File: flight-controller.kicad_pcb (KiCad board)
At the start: 4 copper layers, 36 x 36 mm, 51 parts, among them J1 USB_C_Receptacle_USB2.0, J2 ESC, J3 RX, J4 GPS, J5 I2C, J6 Camera, J7 VTX, J8 DVTX, U1 AT32F435RGT7

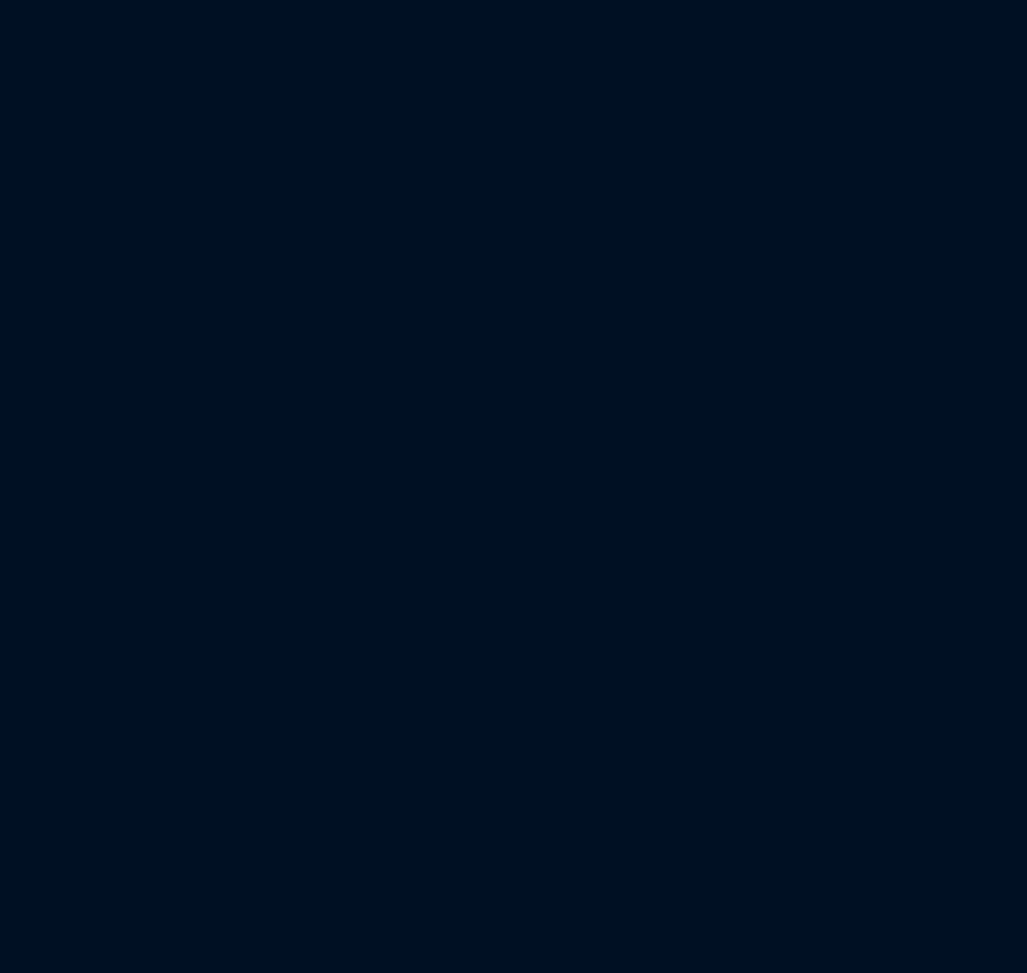
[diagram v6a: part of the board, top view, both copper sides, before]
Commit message: Change baro to I2C
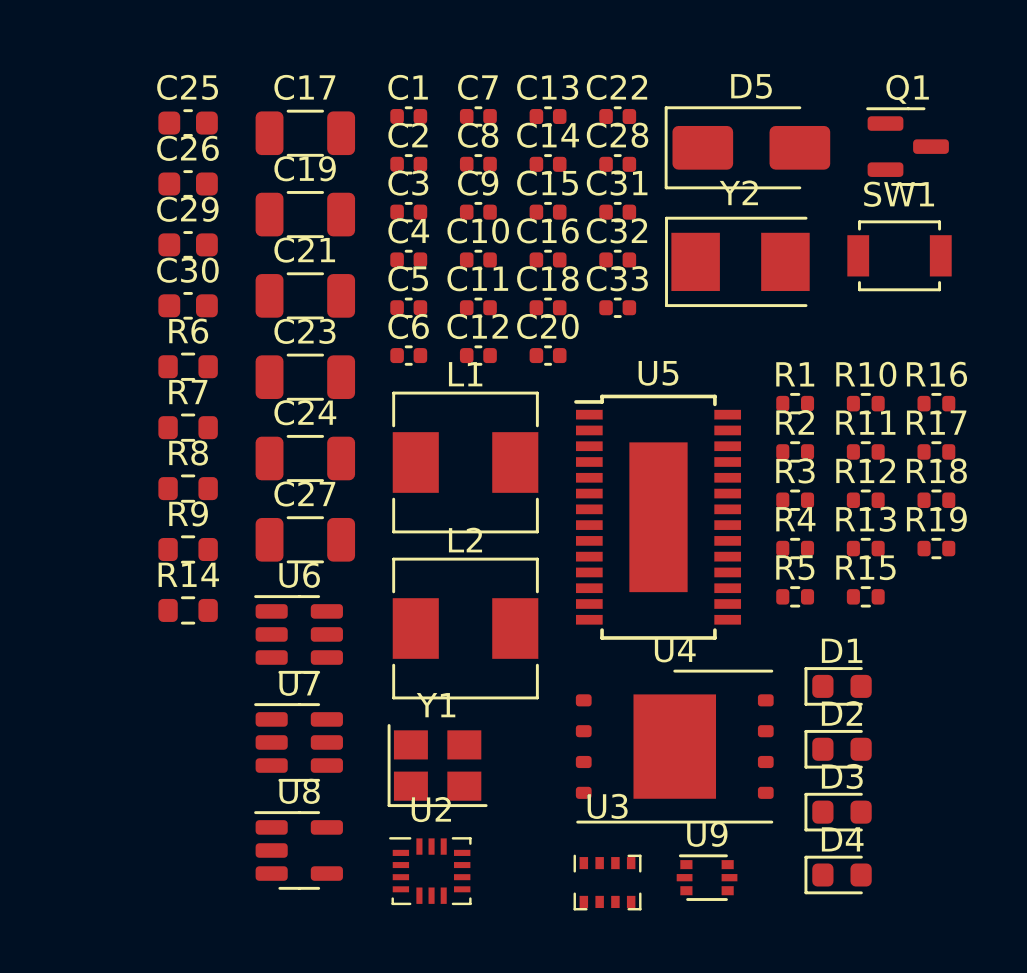
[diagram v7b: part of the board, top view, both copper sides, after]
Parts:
- added C1: 100n, Capacitor_SMD:C_0402_1005Metric, F.Cu at (156.4, 87.8)
- added C10: 100n, Capacitor_SMD:C_0402_1005Metric, F.Cu at (159.2, 93.7)
- added C11: 100n, Capacitor_SMD:C_0402_1005Metric, F.Cu at (159.2, 95.6)
- added C12: 100n, Capacitor_SMD:C_0402_1005Metric, F.Cu at (159.2, 97.6)
- added C13: 100n, Capacitor_SMD:C_0402_1005Metric, F.Cu at (162.1, 87.8)
- added C14: 100n, Capacitor_SMD:C_0402_1005Metric, F.Cu at (162.1, 89.7)
- added C15: 100n, Capacitor_SMD:C_0402_1005Metric, F.Cu at (162.1, 91.7)
- added C16: 68p, Capacitor_SMD:C_0402_1005Metric, F.Cu at (162.1, 93.7)
- added C17: 22u, Capacitor_SMD:C_1206_3216Metric, F.Cu at (152.1, 88.4)
- added C18: 100n, Capacitor_SMD:C_0402_1005Metric, F.Cu at (162.1, 95.6)
- added C19: 10u 50V, Capacitor_SMD:C_1206_3216Metric, F.Cu at (152.1, 91.8)
- added C2: 100n, Capacitor_SMD:C_0402_1005Metric, F.Cu at (156.4, 89.7)
- added C20: 100n, Capacitor_SMD:C_0402_1005Metric, F.Cu at (162.1, 97.6)
- added C21: 10u 50V, Capacitor_SMD:C_1206_3216Metric, F.Cu at (152.1, 95.1)
- added C22: 68p, Capacitor_SMD:C_0402_1005Metric, F.Cu at (165.0, 87.8)
- added C23: 22u, Capacitor_SMD:C_1206_3216Metric, F.Cu at (152.1, 98.5)
- added C24: 22u, Capacitor_SMD:C_1206_3216Metric, F.Cu at (152.1, 101.8)
- added C25: 10u, Capacitor_SMD:C_0603_1608Metric, F.Cu at (147.3, 88.0)
- added C26: 10u, Capacitor_SMD:C_0603_1608Metric, F.Cu at (147.3, 90.5)
- added C27: 22u, Capacitor_SMD:C_1206_3216Metric, F.Cu at (152.1, 105.2)
- added C28: 100n, Capacitor_SMD:C_0402_1005Metric, F.Cu at (165.0, 89.7)
- added C29: 10u, Capacitor_SMD:C_0603_1608Metric, F.Cu at (147.3, 93.0)
- added C3: 100n, Capacitor_SMD:C_0402_1005Metric, F.Cu at (156.4, 91.7)
- added C30: 10u, Capacitor_SMD:C_0603_1608Metric, F.Cu at (147.3, 95.5)
- added C31: 100n, Capacitor_SMD:C_0402_1005Metric, F.Cu at (165.0, 91.7)
- added C32: 22pf, Capacitor_SMD:C_0402_1005Metric, F.Cu at (165.0, 93.7)
- added C33: 22pf, Capacitor_SMD:C_0402_1005Metric, F.Cu at (165.0, 95.6)
- added C4: 100n, Capacitor_SMD:C_0402_1005Metric, F.Cu at (156.4, 93.7)
- added C5: 100n, Capacitor_SMD:C_0402_1005Metric, F.Cu at (156.4, 95.6)
- added C6: 100n, Capacitor_SMD:C_0402_1005Metric, F.Cu at (156.4, 97.6)
- added C7: 100n, Capacitor_SMD:C_0402_1005Metric, F.Cu at (159.2, 87.8)
- added C8: 100n, Capacitor_SMD:C_0402_1005Metric, F.Cu at (159.2, 89.7)
- added C9: 100n, Capacitor_SMD:C_0402_1005Metric, F.Cu at (159.2, 91.7)
- added D1: BLUE, LED_SMD:LED_0603_1608Metric, F.Cu at (174.2, 111.2)
- added D2: GREEN, LED_SMD:LED_0603_1608Metric, F.Cu at (174.2, 113.8)
- added D3: RED, LED_SMD:LED_0603_1608Metric, F.Cu at (174.2, 116.4)
- added D4: YELLOW, LED_SMD:LED_0603_1608Metric, F.Cu at (174.2, 119.0)
- added D5: SS34, Diode_SMD:D_SMA, F.Cu at (170.5, 89.0)
- added L1: 10u, Inductor_SMD:L_Sunlord_MWSA0503S, F.Cu at (158.7, 102.0)
- added L2: 10u, Inductor_SMD:L_Sunlord_MWSA0503S, F.Cu at (158.7, 108.8)
- added Q1: AO3400A, Package_TO_SOT_SMD:SOT-23, F.Cu at (176.9, 89.0)
- added R1: 10k, Resistor_SMD:R_0402_1005Metric, F.Cu at (172.3, 99.6)
- added R10: 100k, Resistor_SMD:R_0402_1005Metric, F.Cu at (175.2, 99.6)
- added R11: 6.34k, Resistor_SMD:R_0402_1005Metric, F.Cu at (175.2, 101.6)
- added R12: 100k, Resistor_SMD:R_0402_1005Metric, F.Cu at (175.2, 103.6)
- added R13: 13.3k, Resistor_SMD:R_0402_1005Metric, F.Cu at (175.2, 105.5)
- added R14: 1k, Resistor_SMD:R_0603_1608Metric, F.Cu at (147.3, 108.1)
- added R15: 75, Resistor_SMD:R_0402_1005Metric, F.Cu at (175.2, 107.5)
- added R16: 75, Resistor_SMD:R_0402_1005Metric, F.Cu at (178.1, 99.6)
- added R17: 100k, Resistor_SMD:R_0402_1005Metric, F.Cu at (178.1, 101.6)
- added R18: 10k, Resistor_SMD:R_0402_1005Metric, F.Cu at (178.1, 103.6)
- added R19: 100k, Resistor_SMD:R_0402_1005Metric, F.Cu at (178.1, 105.5)
- added R2: 5.1k, Resistor_SMD:R_0402_1005Metric, F.Cu at (172.3, 101.6)
- added R3: 5.1k, Resistor_SMD:R_0402_1005Metric, F.Cu at (172.3, 103.6)
- added R4: 10k, Resistor_SMD:R_0402_1005Metric, F.Cu at (172.3, 105.5)
- added R5: 10k, Resistor_SMD:R_0402_1005Metric, F.Cu at (172.3, 107.5)
- added R6: 1k, Resistor_SMD:R_0603_1608Metric, F.Cu at (147.3, 98.1)
- added R7: 220, Resistor_SMD:R_0603_1608Metric, F.Cu at (147.3, 100.6)
- added R8: 220, Resistor_SMD:R_0603_1608Metric, F.Cu at (147.3, 103.1)
- added R9: 2.2k, Resistor_SMD:R_0603_1608Metric, F.Cu at (147.3, 105.6)
- added SW1: SW_Push, Button_Switch_SMD:SW_SPST_B3U-1000P, F.Cu at (176.6, 93.5)
- added U2: BMI270, Package_LGA:Bosch_LGA-14_3x2.5mm_P0.5mm, F.Cu at (157.3, 118.8)
- added U3: BMP280, Package_LGA:Bosch_LGA-8_2x2.5mm_P0.65mm_ClockwisePinNumbering, F.Cu at (164.6, 119.3)
- added U4: W25N01GVZEIG, Package_SON:WSON-8-1EP_8x6mm_P1.27mm_EP3.4x4.3mm, F.Cu at (167.3, 113.7)
- added U5: AT7456E, Package_SO:TSSOP-28-1EP_4.4x9.7mm_P0.65mm, F.Cu at (166.7, 104.3)
- added U6: TPS54302, Package_TO_SOT_SMD:SOT-23-6, F.Cu at (151.9, 109.1)
- added U7: TPS54302, Package_TO_SOT_SMD:SOT-23-6, F.Cu at (151.9, 113.5)
- added U8: TLV75733PDBV, Package_TO_SOT_SMD:SOT-23-5, F.Cu at (151.9, 118.0)
- added U9: USBLC6-2P6, Package_TO_SOT_SMD:SOT-666, F.Cu at (168.7, 119.1)
- added Y1: 27MHz, Crystal:Crystal_SMD_3225-4Pin_3.2x2.5mm, F.Cu at (157.6, 114.5)
- added Y2: 8MHz, Crystal:Crystal_SMD_5032-2Pin_5.0x3.2mm, F.Cu at (170.0, 93.7)
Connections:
- J2 pad 4: UART5_RX -> UART8_RX
- J8 pad 6: UART6_RX -> UART5_RX
- U1 pad 2: 10V_SW -> unconnected-(U1-PC13-Pad2)
- U1 pad 3: BUZZ -> unconnected-(U1-PC14-Pad3)
- U1 pad 53: UART5_TX -> 10V_SW
- U1 pad 54: UART5_RX -> BUZZ
- U1 pad 58: SPI4_CS -> I2C1_SCL
- U1 pad 59: SPI4_SCK -> I2C1_SDA
- U1 pad 61: SPI4_MISO -> UART5_RX
- U1 pad 62: SPI4_MOSI -> UART5_TX

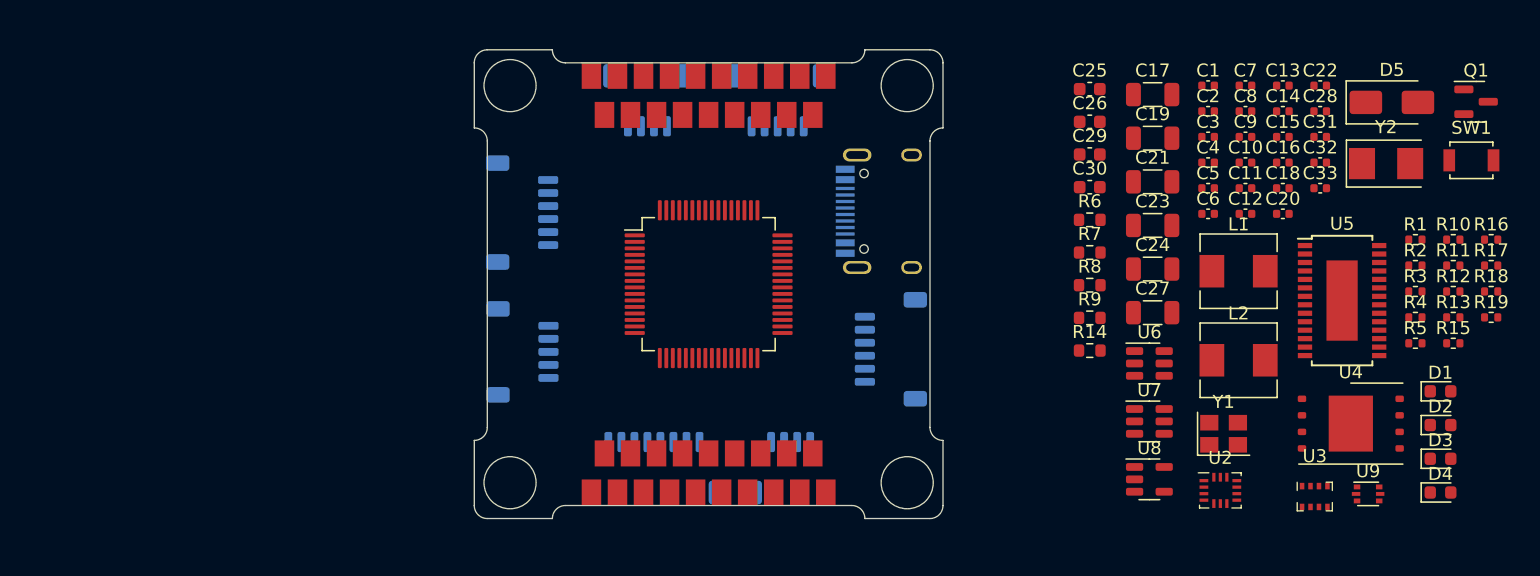
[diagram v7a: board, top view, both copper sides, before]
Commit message: Reduce size of 3v3 regulator capacitors
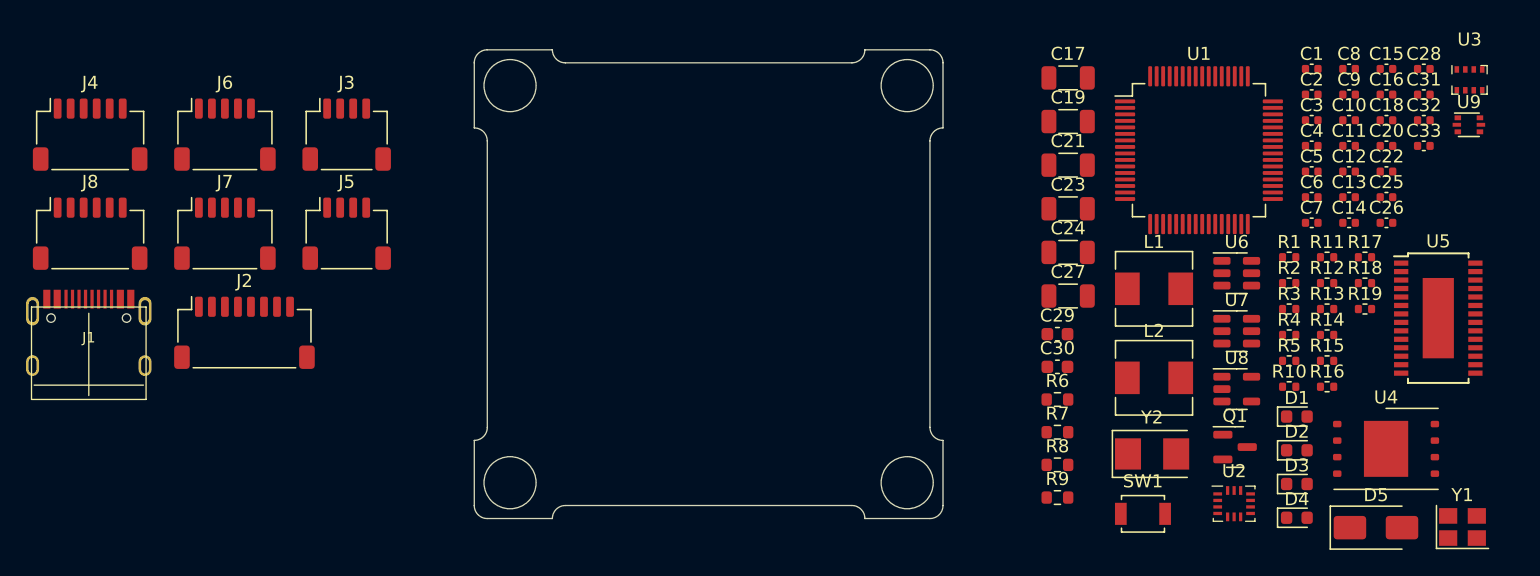
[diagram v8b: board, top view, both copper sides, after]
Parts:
- removed REF** (x38): TestPoint_Pad_1.5x1.5mm, TestPoint:TestPoint_Pad_1.5x1.5mm
- C25, C26: value 10u -> 1u; footprint Capacitor_SMD:C_0603_1608Metric -> Capacitor_SMD:C_0402_1005Metric
- J1, J2, J3, J4, J5, J6, J7, J8: moved to F.Cu
- R14: footprint Resistor_SMD:R_0603_1608Metric -> Resistor_SMD:R_0402_1005Metric
- moved J1 64.3 mm to (70.4, 109.3), turned to 0 degrees
- moved J8 62.1 mm to (70.5, 99.1), turned to 0 degrees
- moved J7 43.7 mm to (80.8, 99.1)
- moved U1 39.0 mm to (155.7, 92.7)
- moved J5 38.6 mm to (90.2, 99.1), turned to 0 degrees
- moved SW1 37.1 mm to (151.4, 120.6)
- moved U3 34.1 mm to (176.4, 87.3)
- moved J4 33.7 mm to (70.5, 91.5), turned to 0 degrees
- moved J2 33.1 mm to (82.3, 106.7), turned to 0 degrees
- moved D5 32.7 mm to (169.3, 121.7)
- moved Q1 32.3 mm to (158.4, 115.5)
- moved U9 29.4 mm to (176.4, 90.8)
- moved Y2 28.6 mm to (152.1, 116.0)
- moved J6 28.3 mm to (80.8, 91.5), turned to 0 degrees
- moved C25 24.3 mm to (170.1, 96.3)
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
